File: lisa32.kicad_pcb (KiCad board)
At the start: 2 copper layers, 1 part, among them J1 USB_C_Receptacle_USB2.0

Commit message: placing test
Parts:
- added C1: 10uF/25V, Capacitor_SMD:C_1206_3216Metric, F.Cu at (118.7, 58.1)
- added C10: 10uF/25V, Capacitor_SMD:C_1206_3216Metric, F.Cu at (93.5, 122.9)
- added C11: 10uF/25V, Capacitor_SMD:C_1206_3216Metric, F.Cu at (108.0, 107.1)
- added C12: 100nF/50V, Capacitor_SMD:C_0603_1608Metric, F.Cu at (107.2, 112.6)
- added C13: 100nF/50V, Capacitor_SMD:C_0603_1608Metric, F.Cu at (96.7, 128.4)
- added C14: 100nF/50V, Capacitor_SMD:C_0603_1608Metric, F.Cu at (105.2, 119.4)
- added C15: 100nF/50V, Capacitor_SMD:C_0603_1608Metric, F.Cu at (92.7, 133.4)
- added C16: 100nF/50V, Capacitor_SMD:C_0603_1608Metric, F.Cu at (110.8, 115.1)
- added C17: 100nF/50V, Capacitor_SMD:C_0603_1608Metric, F.Cu at (96.7, 125.9)
- added C18: 100nF/50V, Capacitor_SMD:C_0603_1608Metric, F.Cu at (116.8, 106.7)
- added C19: 100nF/50V, Capacitor_SMD:C_0603_1608Metric, F.Cu at (92.7, 125.9)
- added C2: 10uF/25V, Capacitor_SMD:C_1206_3216Metric, F.Cu at (113.0, 58.1)
- added C20: 100nF/50V, Capacitor_SMD:C_0603_1608Metric, F.Cu at (125.1, 92.7)
- added C21: 10uF/25V, Capacitor_SMD:C_1206_3216Metric, F.Cu at (125.9, 89.8)
- added C22: 100nF/50V, Capacitor_SMD:C_0603_1608Metric, F.Cu at (125.7, 78.1)
- added C23: 100nF/50V, Capacitor_SMD:C_0603_1608Metric, F.Cu at (100.1, 66.7)
- added C3: 100nF/50V, Capacitor_SMD:C_0603_1608Metric, F.Cu at (118.5, 63.6)
- added C4: 100nF/50V, Capacitor_SMD:C_0603_1608Metric, F.Cu at (122.6, 64.8)
- added C5: 100nF/50V, Capacitor_SMD:C_0603_1608Metric, F.Cu at (119.0, 104.2)
- added C6: 10uF/25V, Capacitor_SMD:C_1206_3216Metric, F.Cu at (102.0, 116.5)
- added C7: 100nF/50V, Capacitor_SMD:C_0603_1608Metric, F.Cu at (101.2, 119.4)
- added C8: 20pF, Capacitor_SMD:C_0603_1608Metric, F.Cu at (98.4, 122.5)
- added C9: 20pF, Capacitor_SMD:C_0603_1608Metric, F.Cu at (115.0, 104.2)
- added D1: BAT760, Diode_SMD:D_SOD-323, F.Cu at (110.4, 62.3)
- added D2: PRTR5V0U2X, Package_TO_SOT_SMD:SOT-143, F.Cu at (124.1, 58.7)
- added D3: LED, LED_SMD:LED_0603_1608Metric, F.Cu at (115.1, 101.7)
- added D4: LED, LED_SMD:LED_0603_1608Metric, F.Cu at (107.2, 110.0)
- added D5: WS2812, LED_SMD:LED_WS2812_PLCC6_5.0x5.0mm_P1.6mm, F.Cu at (73.0, 72.4)
- added J2: Conn_01x19, Connector_PinHeader_2.54mm:PinHeader_1x19_P2.54mm_Vertical, F.Cu at (55.2, 50.8)
- added J3: Conn_01x19, Connector_PinHeader_2.54mm:PinHeader_1x19_P2.54mm_Vertical, F.Cu at (79.4, 50.8)
- added L1: HZ0805E601R-10, Inductor_SMD:L_0603_1608Metric, F.Cu at (92.7, 128.4)
- added L2: HZ0805E601R-10, Inductor_SMD:L_0603_1608Metric, F.Cu at (111.2, 111.7)
- added Q1: SS8050-G, Package_TO_SOT_SMD:SOT-23, F.Cu at (100.9, 63.2)
- added Q2: SS8050-G, Package_TO_SOT_SMD:SOT-23, F.Cu at (105.8, 63.0)
- added R1: 1M, Resistor_SMD:R_0603_1608Metric, F.Cu at (114.5, 63.6)
- added R10: 1k, Resistor_SMD:R_0603_1608Metric, F.Cu at (116.1, 66.1)
- added R11: 1k, Resistor_SMD:R_0603_1608Metric, F.Cu at (126.6, 64.8)
- added R12: 1k, Resistor_SMD:R_0603_1608Metric, F.Cu at (96.1, 66.8)
- added R13: 10k, Resistor_SMD:R_0603_1608Metric, F.Cu at (119.1, 101.6)
- added R14: 10k, Resistor_SMD:R_0603_1608Metric, F.Cu at (92.7, 130.9)
- added R15: 2.2k, Resistor_SMD:R_0603_1608Metric, F.Cu at (102.4, 121.9)
- added R16: 10k, Resistor_SMD:R_0603_1608Metric, F.Cu at (112.8, 109.2)
- added R17: 12k 1%, Resistor_SMD:R_0603_1608Metric, F.Cu at (116.8, 109.2)
- added R18: 1k, Resistor_SMD:R_0603_1608Metric, F.Cu at (102.4, 124.4)
- added R19: 2.2k, Resistor_SMD:R_0603_1608Metric, F.Cu at (112.8, 106.7)
- added R2: 5.1k, Resistor_SMD:R_0603_1608Metric, F.Cu at (96.1, 64.3)
- added R20: 2.2k, Resistor_SMD:R_0603_1608Metric, F.Cu at (106.8, 116.1)
- added R21: 10k, Resistor_SMD:R_0603_1608Metric, F.Cu at (121.7, 78.1)
- added R22: 150, Resistor_SMD:R_0603_1608Metric, F.Cu at (118.5, 61.1)
- added R23: 1k, Resistor_SMD:R_0603_1608Metric, F.Cu at (126.6, 62.3)
- added R3: 5.1k, Resistor_SMD:R_0603_1608Metric, F.Cu at (122.6, 62.3)
- added R4: 10k, Resistor_SMD:R_0603_1608Metric, F.Cu at (114.5, 61.1)
- added R5: 10k, Resistor_SMD:R_0603_1608Metric, F.Cu at (92.1, 67.3)
- added R6: 1k, Resistor_SMD:R_0603_1608Metric, F.Cu at (108.1, 66.5)
- added R7: 1k, Resistor_SMD:R_0603_1608Metric, F.Cu at (104.1, 66.7)
- added R8: 1k, Resistor_SMD:R_0603_1608Metric, F.Cu at (112.1, 68.6)
- added R9: 1k, Resistor_SMD:R_0603_1608Metric, F.Cu at (112.1, 66.1)
- added SW1: BOOT, Button_Switch_SMD:SW_SPST_B3U-1000P, F.Cu at (74.9, 98.4)
- added SW2: RST, Button_Switch_SMD:SW_SPST_B3U-1000P, F.Cu at (59.1, 98.4)
- added U1: ESP32-WROOM-32, RF_Module:ESP32-WROOM-32, F.Cu at (67.3, 57.8)
- added U2: FT2232HL, Package_QFP:LQFP-64_10x10mm_P0.5mm, F.Cu at (66.7, 85.1)
- added U3: LD1117S33TR_SOT223, Package_TO_SOT_SMD:SOT-223-3_TabPin2, F.Cu at (107.4, 85.8)
- added U4: 93C46, Package_SO:SO-8_3.9x4.9mm_P1.27mm, F.Cu at (95.0, 118.0)
- added Y1: 12MHz, Crystal:Crystal_SMD_0603-2Pin_6.0x3.5mm, F.Cu at (109.1, 102.9)
- J1: value USB_C_Receptacle_USB2.0 -> DX07S016JA1R1500
- moved J1 79.6 mm to (66.7, 98.4)
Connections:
- net Net-(J1-PadA1) renamed GND
- net Net-(J1-PadA4) renamed /VBUS
- net Net-(J1-PadA8) renamed no_connect_75
- net Net-(J1-PadB8) renamed no_connect_76
- J1 pad A6: Net-(J1-PadA6) -> /USB_D+
- J1 pad A7: Net-(J1-PadA7) -> /USB_D-
- J1 pad B6: Net-(J1-PadB6) -> /USB_D+
- J1 pad B7: Net-(J1-PadB7) -> /USB_D-
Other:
- board outline added: 27.9 x 54.6 mm

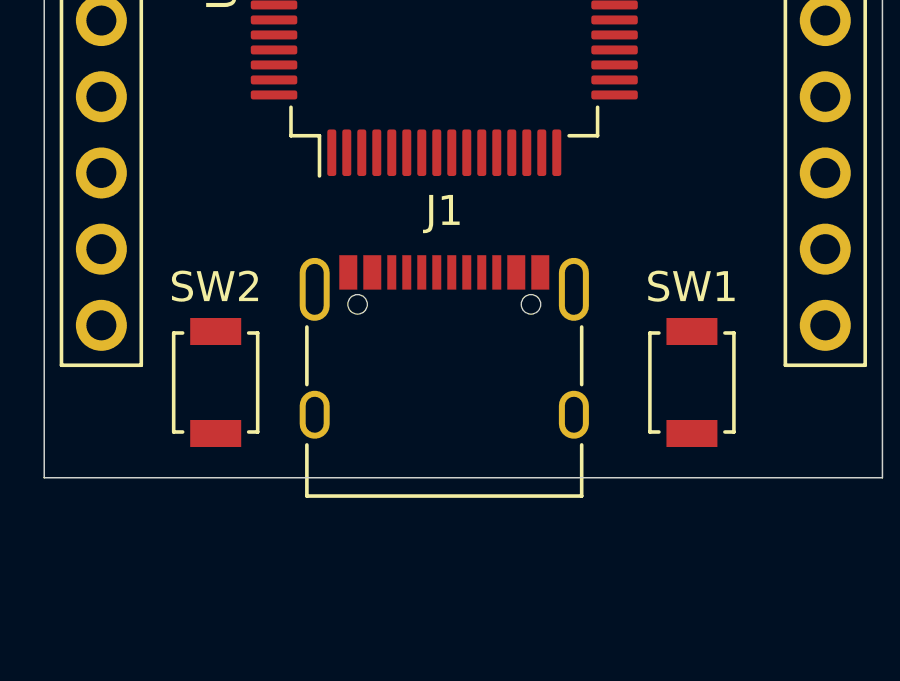
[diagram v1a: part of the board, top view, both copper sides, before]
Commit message: fix autoprogram signals
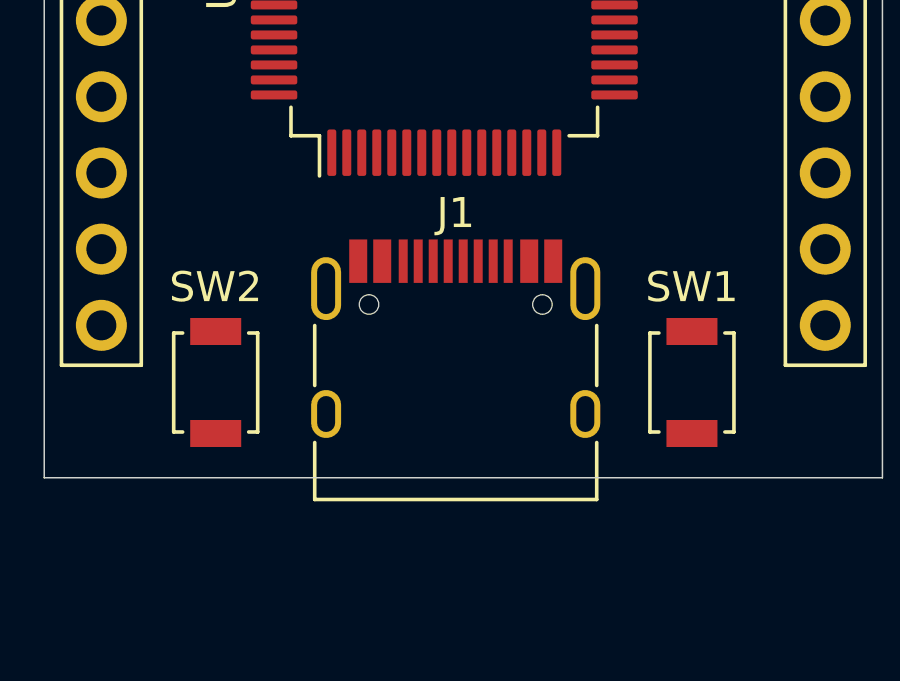
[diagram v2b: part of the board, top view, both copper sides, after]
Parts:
- J1: footprint Connector_USB:USB_C_Receptacle_XKB_U262-16XN-4BVC11 -> Connector_USB:USB_C_Receptacle_HRO_TYPE-C-31-M-12
- moved J1 0.38 mm to (67.1, 98.4)
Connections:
- U2 pad 40: /~DTR -> /~RTS
- U2 pad 43: /~RTS -> /~DTR

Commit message: sch update
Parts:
- D2: moved to B.Cu
- moved D2 68.9 mm to (66.9, 97.3)
- moved U2 0.38 mm to (67.1, 85.1)
- moved SW1 0.25 mm to (75.2, 98.4)
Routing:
- net /USB_D-: track 0.00 -> 3.61 mm
- net /USB_D+: track 0.00 -> 3.61 mm
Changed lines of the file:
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@@
-    )
-  )
-  (footprint "Package_TO_SOT_SMD:SOT-143" (layer "F.Cu")
-    (at 124.075 58.73)
-    (descr "SOT-143")
-    (tags "SOT-143")
-    (property "Sheet file" "lisa32.kicad_sch")
-    (property "Sheet name" "")
-    (attr smd)
-    (fp_text reference "D2" (at 0.02 -2.38) (layer "F.SilkS")
-      (effects (font (size 1 1) (thickness 0.15)))
-    )
-    (fp_text value "PRTR5V0U2X" (at -0.28 2.48) (layer "F.Fab")
-      (effects (font (size 1 1) (thickness 0.15)))
-    )
-    (fp_text user "${REFERENCE}" (at 0 0 90) (layer "F.Fab")
-      (effects (font (size 0.5 0.5) (thickness 0.075)))
-    )
-    (fp_line (start 1.2 -1.55) (end -1.75 -1.55) (layer "F.SilkS") (width 0.12))
-    (fp_line (start -1.2 1.55) (end 1.2 1.55) (layer "F.SilkS") (width 0.12))
-    (fp_line (start 2.05 -1.75) (end -2.05 -1.75) (layer "F.CrtYd") (width 0.05))
-    (fp_line (start -2.05 1.75) (end -2.05 -1.75) (layer "F.CrtYd") (width 0.05))
-    (fp_line (start 2.05 -1.75) (end 2.05 1.75) (layer "F.CrtYd") (width 0.05))
-    (fp_line (start -2.05 1.75) (end 2.05 1.75) (layer "F.CrtYd") (width 0.05))
-    (fp_line (start 1.2 1.5) (end -1.2 1.5) (layer "F.Fab") (width 0.1))
-    (fp_line (start 1.2 -1.5) (end 1.2 1.5) (layer "F.Fab") (width 0.1))
-    (fp_line (start -1.2 -1) (end -0.7 -1.5) (layer "F.Fab") (width 0.1))
-    (fp_line (start -1.2 1.5) (end -1.2 -1) (layer "F.Fab") (width 0.1))
-    (fp_line (start -0.7 -1.5) (end 1.2 -1.5) (layer "F.Fab") (width 0.1))
-    (pad "1" smd rect (at -1.1 -0.77 270) (size 1.2 1.4) (layers "F.Cu" "F.Paste" "F.Mask")
-      (net 1 "GND") (pinfunction "GND"))
-    (pad "2" smd rect (at -1.1 0.95 270) (size 1 1.4) (layers "F.Cu" "F.Paste" "F.Mask")
-      (net 17 "/USB_D+") (pinfunction "I/O1"))
-    (pad "3" smd rect (at 1.1 0.95 270) (size 1 1.4) (layers "F.Cu" "F.Paste" "F.Mask")
-      (net 16 "/USB_D-") (pinfunction "I/O2"))
-    (pad "4" smd rect (at 1.1 -0.95 270) (size 1 1.4) (layers "F.Cu" "F.Paste" "F.Mask")
-      (net 15 "/VBUS") (pinfunction "VCC"))
-    (model "${KISYS3DMOD}/Package_TO_SOT_SMD.3dshapes/SOT-143.wrl"
-      (offset (xyz 0 0 0))
-      (scale (xyz 1 1 1))
-      (rotate (xyz 0 0 0))
     )
   )
@@
   )
   (footprint "Package_QFP:LQFP-64_10x10mm_P0.5mm" (layer "F.Cu")
-    (at 66.675 85.09 90)
+    (at 67.056 85.09 90)
     (descr "LQFP, 64 Pin (https://www.analog.com/media/en/technical-documentation/data-sheets/ad7606_7606-6_7606-4.pdf), generated with kicad-footprint-generator ipc_gullwing_generator.py")
     (tags "LQFP QFP")
@@
   )
   (footprint "Button_Switch_SMD:SW_SPST_B3U-1000P" (layer "F.Cu")
-    (at 74.93 98.425 90)
+    (at 75.184 98.425 90)
     (descr "Ultra-small-sized Tactile Switch with High Contact Reliability, Top-actuated Model, without Ground Terminal, without Boss")
     (tags "Tactile Switch")
@@
     )
   )
+  (footprint "Package_TO_SOT_SMD:SOT-143" (layer "B.Cu")
+    (at 66.929 97.282)
+    (descr "SOT-143")
+    (tags "SOT-143")
+    (property "Sheet file" "lisa32.kicad_sch")
+    (property "Sheet name" "")
+    (attr smd)
+    (fp_text reference "D2" (at 0.02 2.38) (layer "B.SilkS")
+      (effects (font (size 1 1) (thickness 0.15)) (justify mirror))
+    )
+    (fp_text value "PRTR5V0U2X" (at -0.28 -2.48) (layer "B.Fab")
+      (effects (font (size 1 1) (thickness 0.15)) (justify mirror))
+    )
+    (fp_text user "${REFERENCE}" (at 0 0 270) (layer "B.Fab")
+      (effects (font (size 0.5 0.5) (thickness 0.075)) (justify mirror))
+    )
+    (fp_line (start 1.2 1.55) (end -1.75 1.55) (layer "B.SilkS") (width 0.12))
+    (fp_line (start -1.2 -1.55) (end 1.2 -1.55) (layer "B.SilkS") (width 0.12))
+    (fp_line (start 2.05 1.75) (end -2.05 1.75) (layer "B.CrtYd") (width 0.05))
+    (fp_line (start -2.05 -1.75) (end -2.05 1.75) (layer "B.CrtYd") (width 0.05))
+    (fp_line (start 2.05 1.75) (end 2.05 -1.75) (layer "B.CrtYd") (width 0.05))
+    (fp_line (start -2.05 -1.75) (end 2.05 -1.75) (layer "B.CrtYd") (width 0.05))
+    (fp_line (start 1.2 -1.5) (end -1.2 -1.5) (layer "B.Fab") (width 0.1))
+    (fp_line (start 1.2 1.5) (end 1.2 -1.5) (layer "B.Fab") (width 0.1))
+    (fp_line (start -1.2 1) (end -0.7 1.5) (layer "B.Fab") (width 0.1))
+    (fp_line (start -1.2 -1.5) (end -1.2 1) (layer "B.Fab") (width 0.1))
+    (fp_line (start -0.7 1.5) (end 1.2 1.5) (layer "B.Fab") (width 0.1))
+    (pad "1" smd rect (at -1.1 0.77 90) (size 1.2 1.4) (layers "B.Cu" "B.Paste" "B.Mask")
+      (net 1 "GND") (pinfunction "GND"))
+    (pad "2" smd rect (at -1.1 -0.95 90) (size 1 1.4) (layers "B.Cu" "B.Paste" "B.Mask")
+      (net 17 "/USB_D+") (pinfunction "I/O1"))
+    (pad "3" smd rect (at 1.1 -0.95 90) (size 1 1.4) (layers "B.Cu" "B.Paste" "B.Mask")
+      (net 16 "/USB_D-") (pinfunction "I/O2"))
+    (pad "4" smd rect (at 1.1 0.95 90) (size 1 1.4) (layers "B.Cu" "B.Paste" "B.Mask")
+      (net 15 "/VBUS") (pinfunction "VCC"))
+    (model "${KISYS3DMOD}/Package_TO_SOT_SMD.3dshapes/SOT-143.wrl"
+      (offset (xyz 0 0 0))
+      (scale (xyz 1 1 1))
+      (rotate (xyz 0 0 0))
+    )
+  )
   (gr_line (start 53.34 46.99) (end 81.28 46.99) (layer "Edge.Cuts") (width 0.05))
   (gr_line (start 53.34 101.6) (end 53.34 46.99) (layer "Edge.Cuts") (width 0.05))
   (gr_line (start 81.28 46.99) (end 81.28 101.6) (layer "Edge.Cuts") (width 0.05))
   (gr_line (start 81.28 101.6) (end 53.34 101.6) (layer "Edge.Cuts") (width 0.05))
+  (segment (start 66.306 90.765) (end 66.306 94.38) (width 0.2) (layer "F.Cu") (net 16))
+  (segment (start 66.806 94.38) (end 66.806 90.765) (width 0.2) (layer "F.Cu") (net 17))
 )

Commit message: wip placing
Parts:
- added H1: MountingHole, MountingHole:MountingHole_2.2mm_M2, F.Cu at (55.2, 46.5)
- added H2: MountingHole, MountingHole:MountingHole_2.2mm_M2, F.Cu at (79.4, 46.5)
- added H3: MountingHole, MountingHole:MountingHole_2.2mm_M2, F.Cu at (79.4, 100.8)
- added H4: MountingHole, MountingHole:MountingHole_2.2mm_M2, F.Cu at (55.2, 100.8)
- J1: footprint Connector_USB:USB_C_Receptacle_HRO_TYPE-C-31-M-12 -> Connector_USB:USB_C_Receptacle_Palconn_UTC16-G
- R1, R2, R3, U4: moved to B.Cu
- moved R3 64.9 mm to (69.1, 99.1), turned to -90 degrees
- moved R1 61.3 mm to (64.5, 99.1), turned to -90 degrees
- moved D1 59.5 mm to (59.3, 92.8)
- moved R2 45.9 mm to (66.0, 99.1), turned to -90 degrees
- moved U3 45.9 mm to (63.2, 73.4)
- moved U4 43.1 mm to (67.3, 85.0)
- moved D2 2.42 mm to (67.1, 94.9)
- moved U2 2.05 mm to (67.3, 87.1)
- moved SW2 0.81 mm to (59.7, 97.9)
- moved J1 0.25 mm to (67.3, 98.4)
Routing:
- net /USB_D-: track 3.61 -> 0.00 mm
- net /USB_D+: track 3.61 -> 0.00 mm
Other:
- board size 27.9 x 54.6 mm -> 27.9 x 58.2 mm

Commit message: routing completed
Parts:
- C11, C15, C16, C17, C19, C20, C21, C22, C5, C7, L1, L2, Q1, Q2, R17, R19, R20, R21, R4, R5, R6, R7: moved to B.Cu
- J1: value DX07S016JA1R1500 -> USB4105-GF-A
- Y1: footprint Crystal:Crystal_SMD_0603-2Pin_6.0x3.5mm -> Crystal:Crystal_SMD_3225-4Pin_3.2x2.5mm
- moved C21 144.8 mm to (7.11, 6.99)
- moved C20 141.4 mm to (11.0, 9.14)
- moved C22 140.0 mm to (6.35, 4.95)
- moved R21 129.6 mm to (11.0, 10.8), turned to 180 degrees
- moved R15 128.4 mm to (6.30, 36.7)
- moved C18 128.1 mm to (14.3, 29.8), turned to 90 degrees
- moved R16 127.9 mm to (6.30, 38.5)
- moved R13 127.6 mm to (6.30, 41.9)
- moved C14 126.0 mm to (16.5, 29.8), turned to 90 degrees
- moved R14 125.3 mm to (6.30, 40.2)
- moved L2 125.0 mm to (6.25, 43.9)
- moved C11 124.9 mm to (9.02, 31.0), turned to 90 degrees
- moved C5 122.5 mm to (12.7, 43.3), turned to 180 degrees
- moved C15 121.9 mm to (9.04, 44.8), turned to -90 degrees
- moved C19 121.4 mm to (12.2, 35.0)
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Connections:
- D5 pad 1: no_connect_74 -> no_connect_75
- J1 pad A8: no_connect_75 -> no_connect_76
- J1 pad B8: no_connect_76 -> no_connect_77
- R20 pad 1: /USB to JTAG + UART/~RXLED -> /USB to JTAG + UART/~TXLED
- U2 pad 21: no_connect_77 -> no_connect_78
- U2 pad 23: no_connect_78 -> no_connect_79
- U2 pad 24: no_connect_79 -> no_connect_80
- U2 pad 26: no_connect_80 -> no_connect_81
- U2 pad 27: no_connect_81 -> no_connect_82
- U2 pad 28: no_connect_82 -> no_connect_83
- U2 pad 29: no_connect_83 -> no_connect_84
- U2 pad 30: no_connect_84 -> no_connect_85
- U2 pad 32: no_connect_85 -> no_connect_86
- U2 pad 33: no_connect_86 -> no_connect_87
- U2 pad 34: no_connect_87 -> no_connect_88
- U2 pad 36: no_connect_88 -> no_connect_89
- U2 pad 48: no_connect_89 -> no_connect_90
- U2 pad 52: no_connect_90 -> no_connect_91
- U2 pad 53: no_connect_91 -> no_connect_92
- U2 pad 55: /USB to JTAG + UART/~RXLED -> /USB to JTAG + UART/~TXLED
- U2 pad 57: no_connect_92 -> no_connect_93
- U2 pad 58: no_connect_93 -> no_connect_94
- U2 pad 59: no_connect_94 -> no_connect_95
- U2 pad 60: no_connect_95 -> no_connect_96
- Y1 pad 2: Net-(C8-Pad2) -> GND
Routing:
- net +3V3: track 0.00 -> 137.6 mm, vias 0 -> 7
- net GND: track 0.00 -> 120.3 mm, vias 0 -> 26
- net /EN: track 0.00 -> 102.4 mm, vias 0 -> 2
- net /IO14: track 0.00 -> 92.9 mm, vias 0 -> 1
- net /IO13: track 0.00 -> 69.0 mm, vias 0 -> 2
- net /IO12: track 0.00 -> 58.0 mm, vias 0 -> 2
- net +5V: track 0.00 -> 58.0 mm, vias 0 -> 4
- net /IO0: track 0.00 -> 51.2 mm, vias 0 -> 1
- net /USB to JTAG + UART/VREG: track 0.00 -> 43.5 mm, vias 0 -> 5
- net /CLK: track 0.00 -> 41.2 mm, vias 0 -> 1
- net /CMD: track 0.00 -> 38.3 mm, vias 0 -> 1
- net /SD0: track 0.00 -> 38.1 mm, vias 0 -> 1
- net /SD3: track 0.00 -> 35.0 mm, vias 0 -> 1
- net /IO15: track 0.00 -> 34.1 mm, vias 0 -> 1
- net /SD1: track 0.00 -> 33.6 mm, vias 0 -> 1
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- added copper zone on B.Cu, net GND
- added copper zone on F.Cu, net GND
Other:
- board size 27.9 x 58.2 mm -> 29.1 x 58.3 mm

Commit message: v0.1.0
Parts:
- added G***: LOGO, LOGO, F.Cu at (23.5, 49.0)
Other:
- board text added: "0"
- board text added: "12"
- board text added: "13"
- board text added: "14"
- board text added: "15"
- board text added: "16"
- board text added: "17"
- board text added: "18"
- board text added: "19"
- board text added: "2"
- board text added: "21"
- board text added: "22"
- board text added: "23"
- board text added: "25"
- board text added: "26"
- board text added: "27"
- board text added: "32"
- board text added: "33"
- board text added: "34"
- board text added: "35"
- board text added: "3V3"
- board text added: "4"
- board text added: "5"
- board text added: "5V"
- board text added: "CK"
- board text added: "CMD"
- board text added: "D0"
- board text added: "D1"
- board text added: "D2"
- board text added: "D3"
- board text added: "EN"
- board text added: "G"
- board text added: "RX"
- board text added: "TX"
- board text added: "VN"
- board text added: "VP"

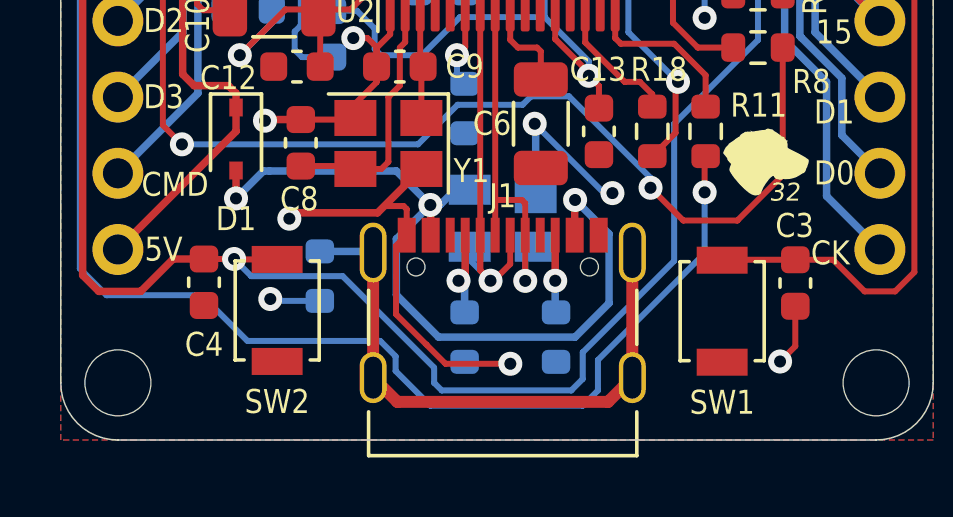
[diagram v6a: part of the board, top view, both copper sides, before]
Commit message: readme and button labels
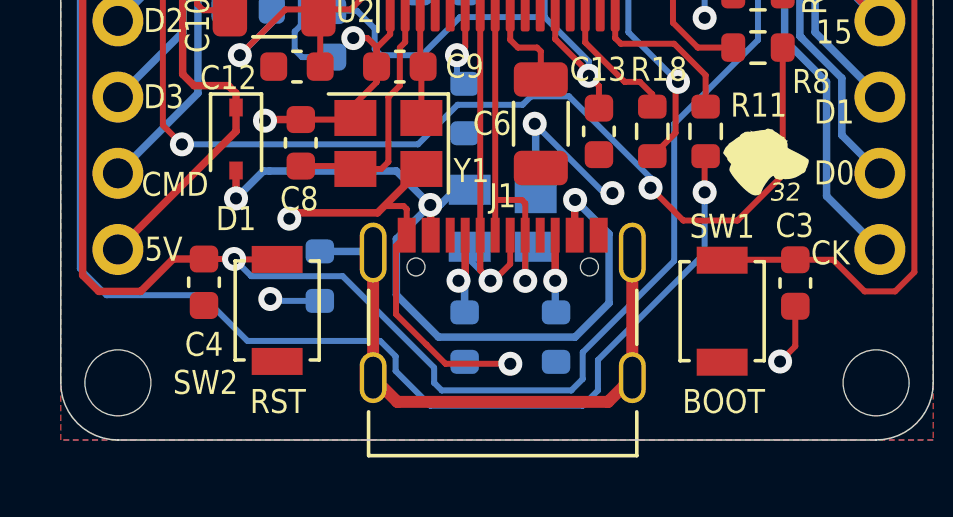
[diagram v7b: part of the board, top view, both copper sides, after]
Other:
- board text added: "BOOT"
- board text added: "RST"
